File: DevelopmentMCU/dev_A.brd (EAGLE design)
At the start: 160 x 100 mm, 36 parts, among them U1 TM4C123_DEVICE, U3 3.3V, Y1 32kHz, Y2 Y2

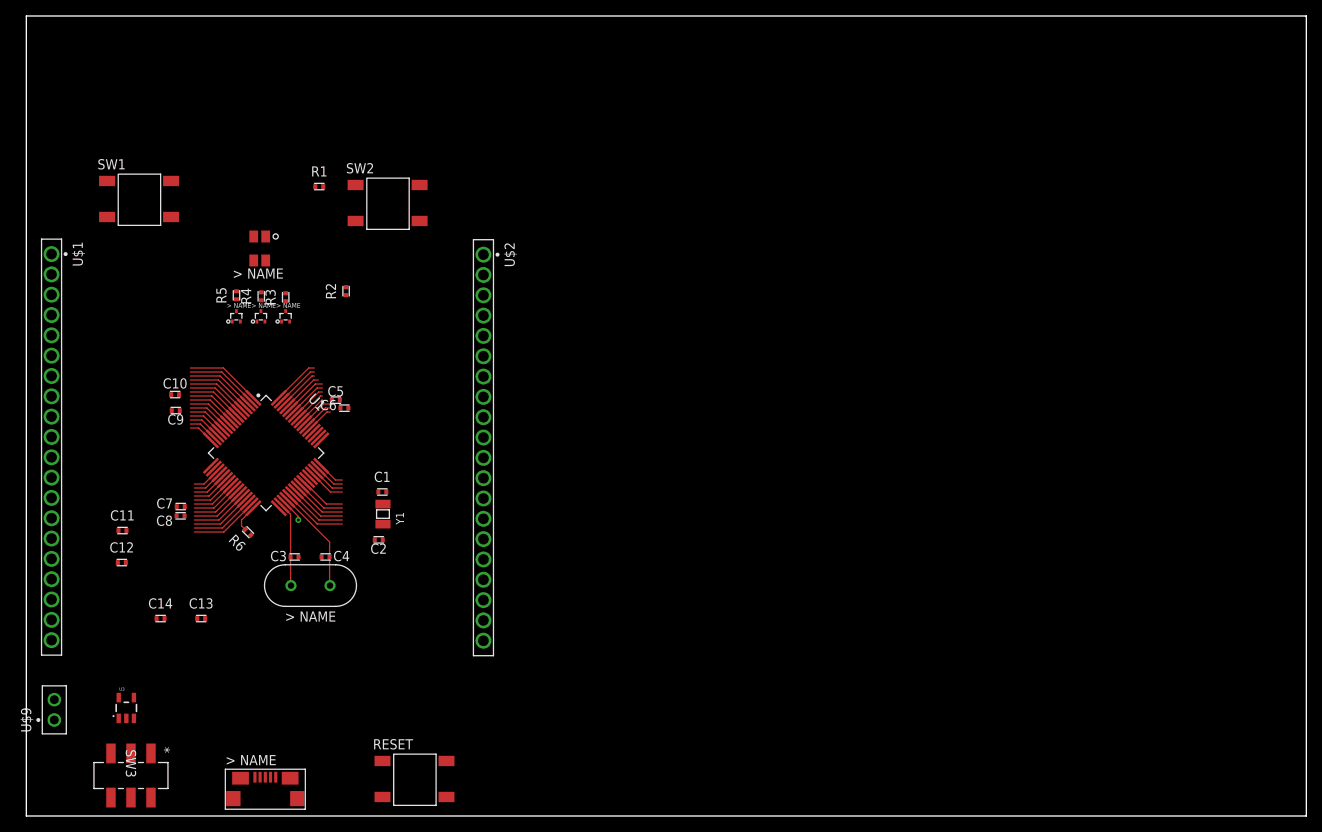
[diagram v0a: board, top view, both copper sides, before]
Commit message: Started on the Fill Control Design, finished with dev MCU
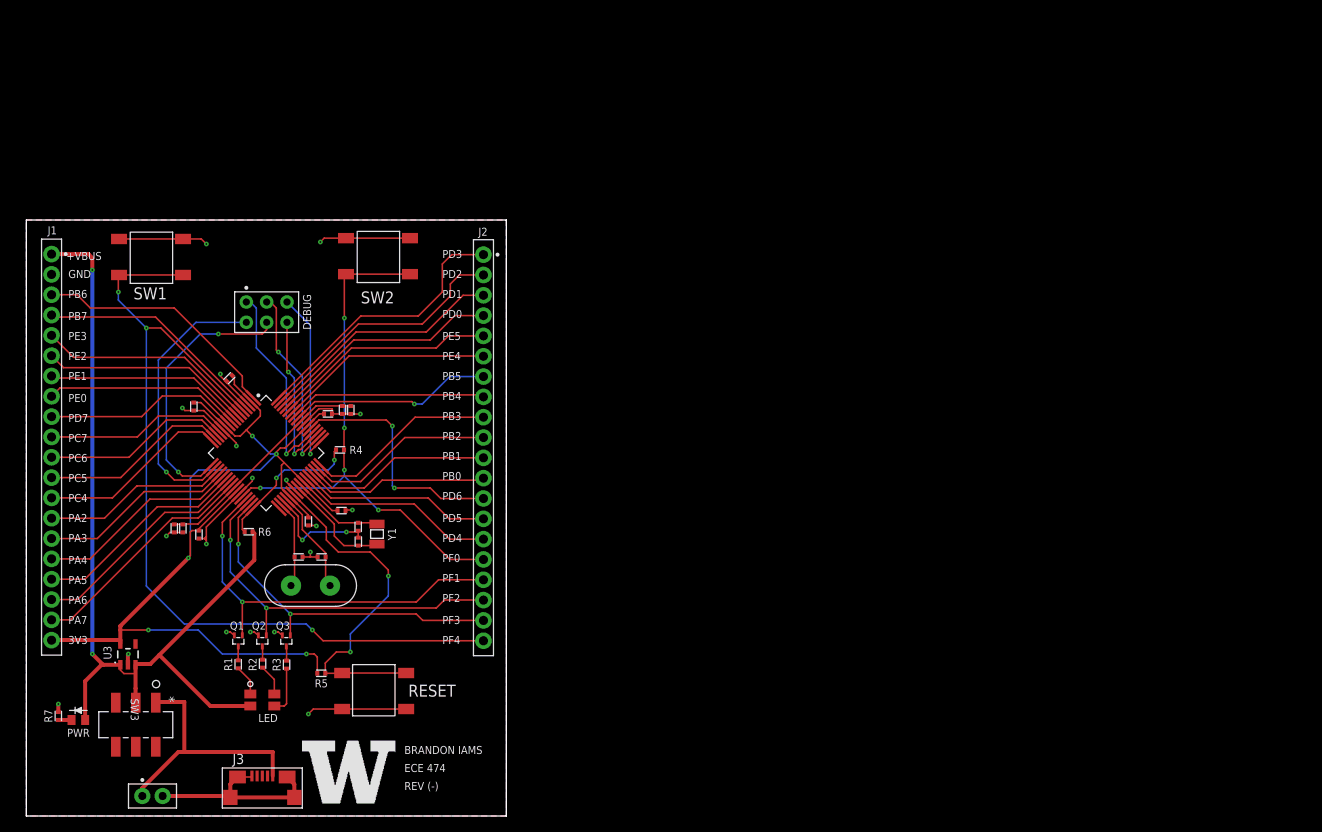
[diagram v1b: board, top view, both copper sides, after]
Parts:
- removed U$3, U$5, U$6: (no value), MICROCONTROLLER:SOT416
- removed U$4: (no value), MICROCONTROLLER:RGBLED
- removed U$8: (no value), MICROCONTROLLER:USBMICROB
- removed U$9: (no value), MICROCONTROLLER:HDRV2W64P254_1X2_600X300X838B
- added DEBUG: (no value), MICROCONTROLLER:HDRV6W64P254_2X3_800X508X838B
- added J1: (no value), MICROCONTROLLER:HDRV20W80P254_1X20_5100X250X838B
- added J3: (no value), MICROCONTROLLER:USBMICROB
- added LED: (no value), MICROCONTROLLER:RGBLED
- added PWR: (no value), MICROCONTROLLER:LED_511
- added Q1, Q2, Q3: (no value), MICROCONTROLLER:SOT416
- added R7: 10k, MICROCONTROLLER:CAPC1005X35N
- added VBUS: (no value), MICROCONTROLLER:HDRV2W64P254_1X2_600X300X838B
- R2: value 10k -> 330
- R4, R5: value 330 -> (none)
- U$1: value (none) -> LOGO; device MICROCONTROLLER:HDRV20W80P254_1X20_5100X250X838B -> MICROCONTROLLER:LOGO
- moved U$1 76.0 mm to (34.5, 1.00), turned to 0 degrees
- moved R1 60.6 mm to (26.5, 19.0), turned to 270 degrees
- moved R5 48.4 mm to (36.9, 17.8), turned to 180 degrees
- moved R2 47.7 mm to (29.5, 19.0), turned to 270 degrees
- moved R3 45.9 mm to (32.5, 18.9), turned to 270 degrees
- moved C14 31.2 mm to (25.4, 54.7), turned to 45 degrees
- moved C5 25.8 mm to (18.5, 36.0), turned to 90 degrees
- moved C10 25.4 mm to (39.4, 38.2), turned to 180 degrees
- moved C8 25.1 mm to (40.6, 50.8), turned to 90 degrees
- moved R4 21.6 mm to (39.2, 45.8), turned to 0 degrees
- moved C12 21.5 mm to (20.9, 51.2), turned to 90 degrees
- moved C9 19.0 mm to (37.7, 50.3), turned to 180 degrees
- moved C13 18.1 mm to (35.3, 36.8), turned to 90 degrees
- moved RESET 12.1 mm to (43.5, 15.6), turned to 180 degrees
- moved C11 9.57 mm to (21.6, 35.2), turned to 90 degrees
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- renumbered U$2 to J2
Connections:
- removed net N$1: U$1.3, U1.19
- removed net N$2: U$1.4, U1.20
- removed net N$44: SW3.1, U$8.VB
- new net +VBUS_IN: J3.VB, SW3.1, VBUS.1
- new net N$43: DEBUG.5, U1.17
- new net N$45: DEBUG.6, U1.18
- new net N$46: DEBUG.1, U1.52
- new net N$47: DEBUG.4, U1.51
- new net N$48: DEBUG.2, U1.50
- new net N$49: DEBUG.3, U1.49
- new net N$50: J2.2, U1.63
- new net N$51: J2.1, U1.64
- new net PB6: J1.3, U1.1
- new net PB7: J1.4, U1.4
- net !RST: now also R5.1, RESET.2; no longer J2.20, R2.1, RESET.4
- net !WAKE: now also R4.1; no longer R1.1
- net +3V3: now also J1.20, R5.2; no longer J2.1, R2.2
- net +VBUS: now also J1.1, LED.4, PWR.P$2; no longer U$1.1, U$4.4, U$9.1
- net GND: now also J1.2, J3.0, J3.01, J3.02, J3.03, J3.GND, Q1.2, Q2.2, Q3.2, R7.1, RESET.4, SW1.4, SW2.4, U3.2, VBUS.2; no longer J2.2, RESET.2, SW1.2, SW2.2, U$1.2, U$3.2, U$5.2, U$6.2, U$8.0, U$8.01, U$8.02, U$8.03, U$8.GND, U$9.2
- net LED_B: now also J2.18, Q2.1; no longer J2.17, U$5.1
- net LED_G: now also J2.19, Q3.1; no longer J2.18, U$6.1
- net LED_R: now also J2.17, Q1.1; no longer J2.16, U$3.1
- net N$10: now also J1.12, U1.15; no longer U$1.12, U1.48
- net N$11: now also J1.13, U1.16; no longer U$1.13, U1.58
- net N$12: now also J1.14, U1.19; no longer U$1.14, U1.57
- net N$13: now also J1.15, U1.20; no longer U$1.15, U1.1
- net N$14: now also J1.16, U1.21; no longer U$1.16, U1.4
- net N$15: now also J1.17, U1.22; no longer U$1.17, U1.16
- net N$16: now also J1.18, U1.23; no longer U$1.18, U1.15
- net N$17: now also J1.19, U1.24; no longer U$1.19, U1.14
- net N$18: now also J2.15, U1.43; no longer U$1.20, U1.13
- net N$19: now also J2.14, U1.44; no longer J2.3, U1.61
- net N$20: now also J2.13, U1.53; no longer J2.4, U1.62
- net N$21: now also J2.12, U1.45; no longer J2.5, U1.63
- net N$22: now also J2.11, U1.46; no longer J2.6, U1.64
- net N$23: now also J2.10, U1.47; no longer J2.7, U1.53
- net N$24: now also J2.9, U1.48; no longer J2.8, U1.10
- net N$25: now also J2.8, U1.58; no longer J2.9, U1.9
- net N$26: now also J2.7, U1.57; no longer J2.10, U1.8
- net N$27: now also J2.6, U1.59; no longer J2.11, U1.7
- net N$28: now also J2.5, U1.60; no longer J2.12, U1.6
- net N$29: now also J2.4, U1.61; no longer J2.13, U1.59
- net N$3: now also J1.5, U1.6; no longer U$1.5, U1.21
- net N$30: now also J2.3, U1.62; no longer J2.14, U1.60
- net N$31: now also PWR.P$1, R7.2; no longer U3.2
- net N$32: now also LED.1, R1.2; no longer R3.2, U$4.1
- net N$33: now also LED.2, R2.2; no longer R4.2, U$4.2
- net N$34: now also LED.3, R3.2; no longer R5.2, U$4.3
- net N$35: now also Q3.3, R3.1; no longer R5.1, U$6.3
- net N$36: now also Q2.3, R2.1; no longer R4.1, U$5.3
- net N$37: now also Q1.3, R1.1; no longer R3.1, U$3.3
- net N$4: now also J1.6, U1.7; no longer U$1.6, U1.22
- net N$5: now also J1.7, U1.8; no longer U$1.7, U1.23
- net N$6: now also J1.8, U1.9; no longer U$1.8, U1.24
- net N$7: now also J1.9, U1.10; no longer U$1.9, U1.45
- net N$8: now also J1.10, U1.13; no longer U$1.10, U1.46
- net N$9: now also J1.11, U1.14; no longer U$1.11, U1.47
- net SW1: now also J2.20, SW1.2; no longer J2.19, SW1.4
- net SW2: now also J2.16, R4.2, SW2.2; no longer J2.15, R1.2, SW2.4
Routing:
- net +VBUS: track 0.00 -> 117.3 mm, vias 0 -> 2
- net SW1: track 7.77 -> 109.5 mm, vias 0 -> 3
- net +3V3: track 38.3 -> 134.7 mm, vias 0 -> 5
- net GND: track 31.6 -> 108.4 mm, vias 0 -> 19
- net SW2: track 7.16 -> 68.9 mm, vias 0 -> 5
- net LED_R: track 7.58 -> 50.5 mm, vias 0 -> 2
- net LED_B: track 7.99 -> 46.9 mm, vias 0 -> 2
- net !RST: track 7.51 -> 44.6 mm, vias 0 -> 2
- net LED_G: track 8.41 -> 44.0 mm, vias 0 -> 2
- net N$51: track 0.00 -> 35.0 mm
- net N$45: track 0.00 -> 34.3 mm, vias 0 -> 1
- net N$43: track 0.00 -> 33.9 mm, vias 0 -> 2
- net N$50: track 0.00 -> 32.6 mm
- net +VBUS_IN: track 0.00 -> 32.0 mm
- net PB6: track 0.00 -> 31.4 mm
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- added copper zone on layer 16, net GND
- added copper zone on layer 1, net TOP
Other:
- board size 160 x 100 mm -> 60 x 74.5 mm
- board text added: "+VBUS"
- board text added: "3V3"
- board text added: "BRANDON IAMS"
- board text added: "ECE 474"
- board text added: "GND"
- board text added: "PA2"
- board text added: "PA3"
- board text added: "PA4"
- board text added: "PA5"
- board text added: "PA6"
- board text added: "PA7"
- board text added: "PB0"
- board text added: "PB1"
- board text added: "PB2"
- board text added: "PB3"
- board text added: "PB4"
- board text added: "PB5"
- board text added: "PB6"
- board text added: "PB7"
- board text added: "PC4"
- board text added: "PC5"
- board text added: "PC6"
- board text added: "PC7"
- board text added: "PD0"
- board text added: "PD1"
- board text added: "PD2"
- board text added: "PD3"
- board text added: "PD4"
- board text added: "PD5"
- board text added: "PD6"
- board text added: "PD7"
- board text added: "PE0"
- board text added: "PE1"
- board text added: "PE2"
- board text added: "PE3"
- board text added: "PE4"
- board text added: "PE5"
- board text added: "PF0"
- board text added: "PF1"
- board text added: "PF2"
- board text added: "PF3"
- board text added: "PF4"
- board text added: "REV (-)"
